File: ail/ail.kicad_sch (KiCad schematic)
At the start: 28 parts, among them J1 TS HV-, J2 TS HV+, J8 LED, Q8 FQD1N80TM, Q9 XP262N7002TR-G, U6 OP777

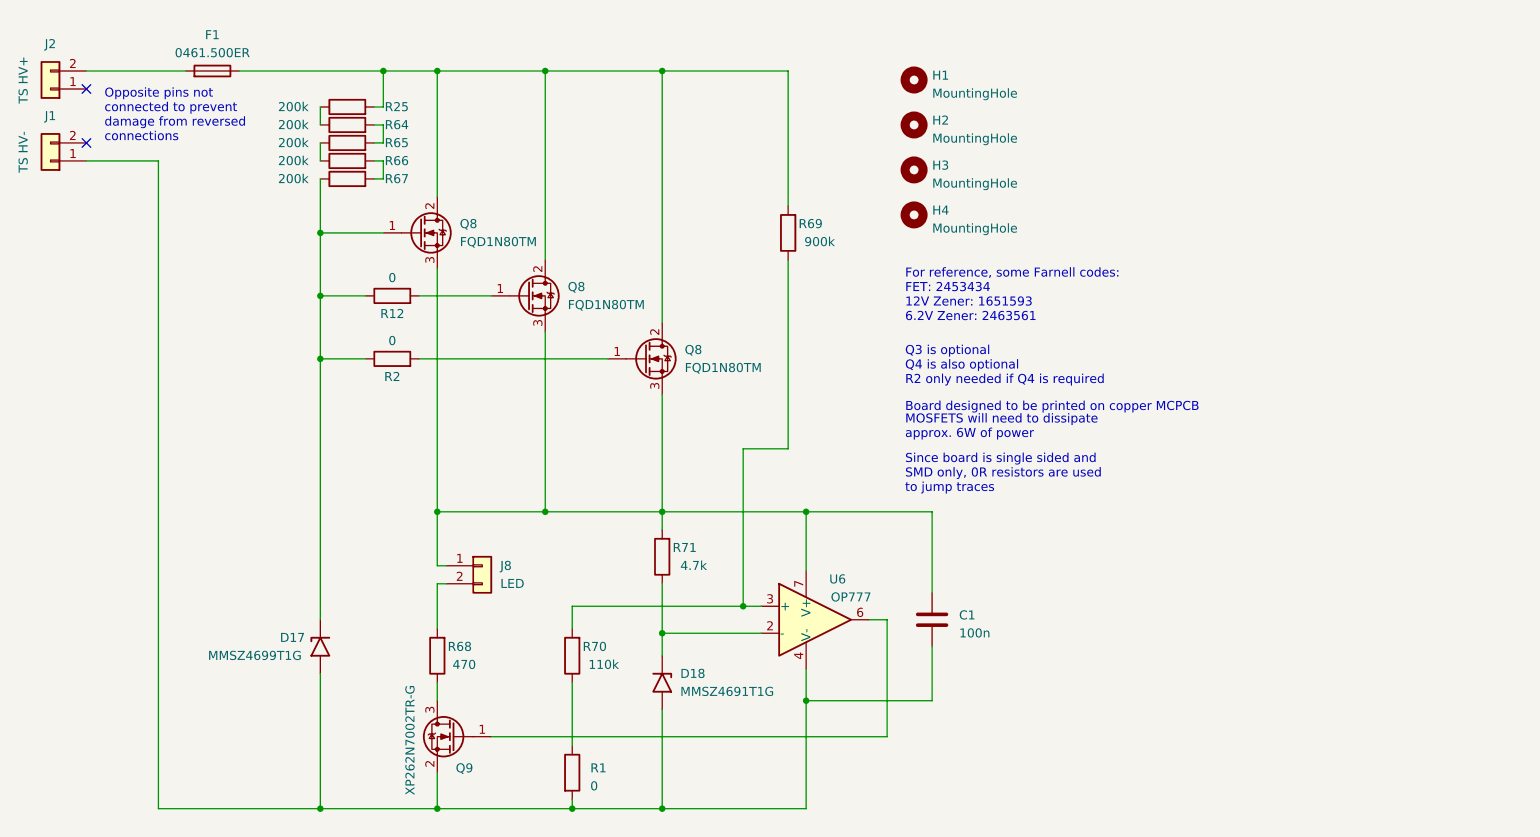
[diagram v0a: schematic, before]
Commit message: fix(ail): corrected remaining ERC errors
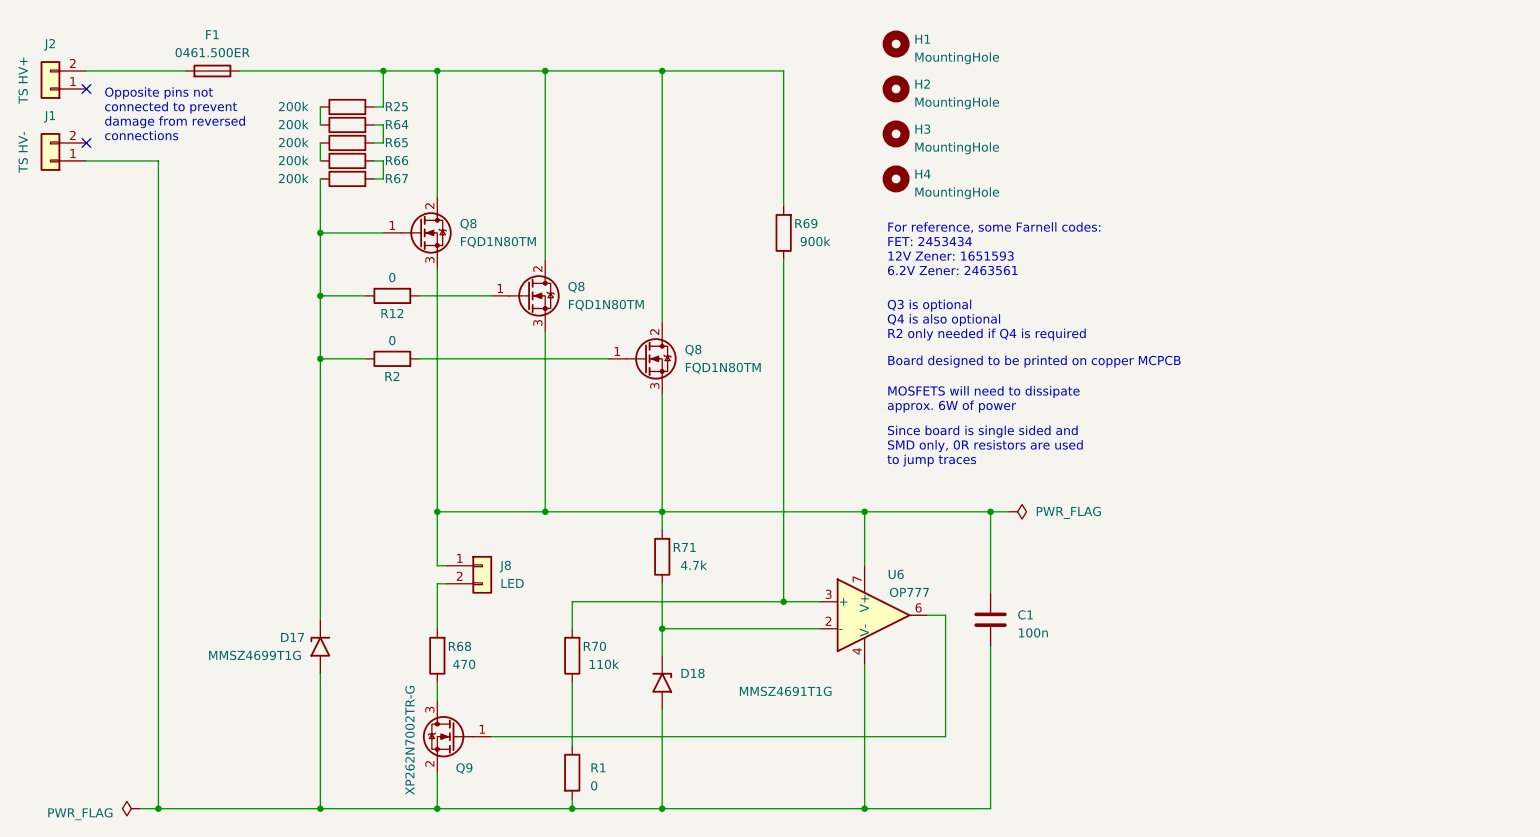
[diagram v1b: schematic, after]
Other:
- moved on the sheet: C1, H1, H2, H3, H4, R69, U6

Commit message: feat(ail): add copper pour to MOSFET drains (#95)
* Added copper pour to Q1-drain, removed R1

* fix(ail): remove track stubs

* wip(ail): attempt to fix clearance issues

not successfully...

* fix(ail): corrected clearance violation for isolation slot

* fix(ail): removed thermal relief for mosfet pour, increased size slightly

* fix(ail): replaced out of stock components

---------

Co-authored-by: Max O'Brien <max@maxobrien.co.uk>
Co-authored-by: Ray Wang <114954263+saltyboi2995@users.noreply.github.com>
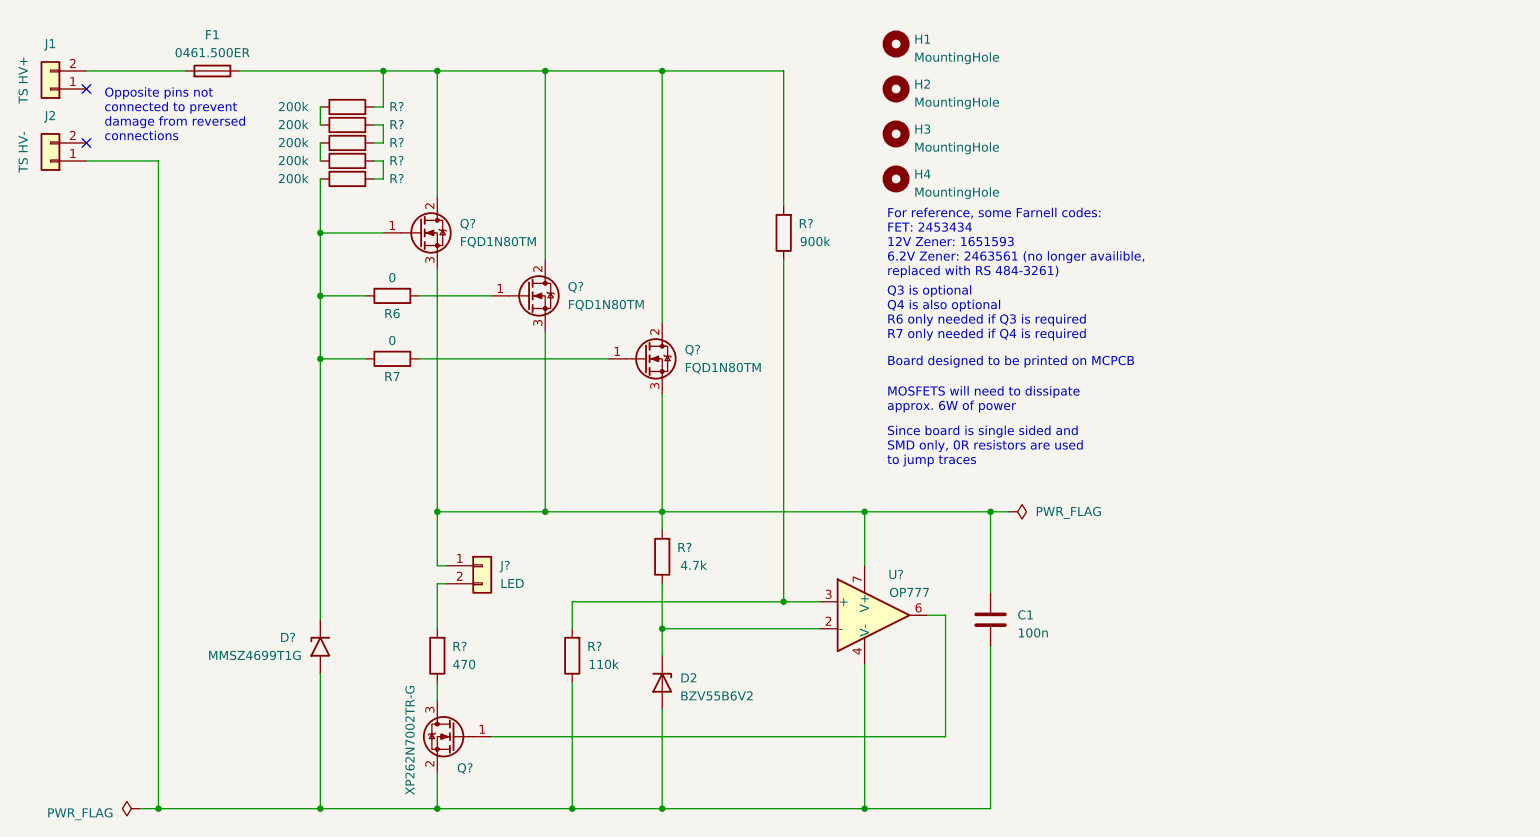
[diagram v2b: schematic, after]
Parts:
- removed D18: MMSZ4691T1G, Diode_SMD:D_SOD-123, symbol Diode:1N630xA
- removed R1: 0, Resistor_SMD:R_1206_3216Metric_Pad1.30x1.75mm_HandSolder, symbol Device:R
- added D2: BZV55B6V2, Diode_SMD:D_MiniMELF, symbol Diode:BZV55B6V2
- renumbered D17 to D?, J2 to J1, J1 to J2, J8 to J?, Q8 to Q?, Q9 to Q?, R12 to R6, R2 to R7, R65 to R?, R25 to R?, R67 to R?, R69 to R?, R71 to R?, R64 to R?, R68 to R?, R66 to R?, R70 to R?, U6 to U?
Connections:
- net at R?.1: now also C1.2, D?.2 (A2), J2.1 (Pin_1), Q?.2 (S), U?.4 (V-), D2.2 (A)
- net at R?.1, U?.2 (-): now also D2.1 (K)
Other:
- note added: "Board designed to be printed on MCPCB"
- note added: "For reference, some Farnell codes: FET: 2453434 12V Zener: 1651593 6.2V Zener: 2463561 (no longer availible, replaced with RS 484-3261)"
- note added: "Q3 is optional Q4 is also optional R6 only needed if Q3 is required R7 only needed if Q4 is required"
- note removed: "Board designed to be printed on copper MCPCB"
- note removed: "For reference, some Farnell codes: FET: 2453434 12V Zener: 1651593 6.2V Zener: 2463561"
- note removed: "Q3 is optional Q4 is also optional R2 only needed if Q4 is required"

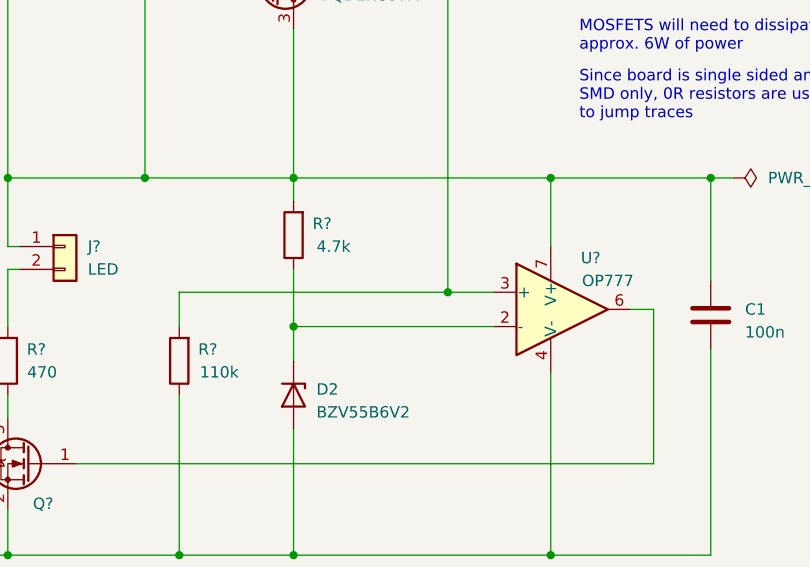
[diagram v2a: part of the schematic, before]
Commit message: Added message about missing clamp on non-inverting input of op-amp
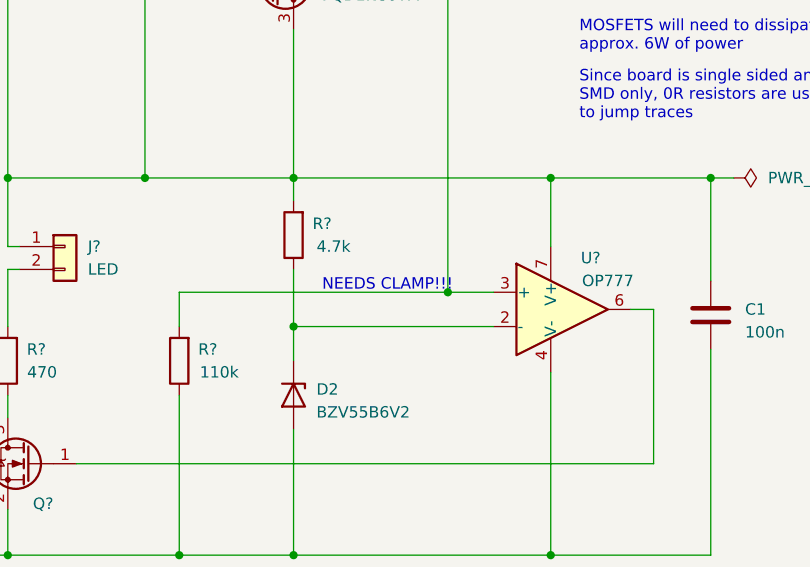
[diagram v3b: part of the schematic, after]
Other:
- note added: "NEEDS CLAMP!!!"
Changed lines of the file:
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@@
     (effects (font (size 1.27 1.27)) (justify left bottom))
+  )
+  (text "NEEDS CLAMP!!!" (at 109.855 97.79 0)
+    (effects (font (size 1.27 1.27) (color 255 0 0 1)) (justify left bottom))
   )
   (text "MOSFETS will need to dissipate \napprox. 6W of power"

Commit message: Added TODO tasks
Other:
- note added: "AIL TODO: - Clamp on op-amp - Choose heat sink"
- note removed: "NEEDS CLAMP!!!"
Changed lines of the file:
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@@
     (effects (font (size 1.27 1.27)) (justify left bottom))
   )
-  (text "NEEDS CLAMP!!!" (at 109.855 97.79 0)
+  (text "AIL TODO:\n- Clamp on op-amp\n- Choose heat sink" (at 205.105 38.1 0)
     (effects (font (size 1.27 1.27) (color 255 0 0 1)) (justify left bottom))
   )

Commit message: Updated schematics
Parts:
- removed R?: 900k, Resistor_SMD:R_0603_1608Metric, symbol Device:R
- added D?: MMSZ5239B, Diode_SMD:D_SOD-123, symbol Diode:1N630xA
- added R? (x4): 200k, Resistor_SMD:R_0805_2012Metric, symbol Device:R
- added R?: 100k, Resistor_SMD:R_0805_2012Metric, symbol Device:R
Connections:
- net at F1.1, Q?.2 (D), Q?.2 (D)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: now also R?.2
- net at R?.2, U?.3 (+): now also D?.1 (A1), R?.1
- net at C1.2, D2.2 (A), D?.2 (A2)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: now also D?.2 (A2)
- new net: R?.1, R?.1 (x2)
- new net: R?.2, R?.2 (x2)
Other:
- moved on the sheet: H1, H2, H3, H4

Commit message: Tweaks
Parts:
- added R? (x3): 10, Resistor_SMD:R_0603_1608Metric, symbol Device:R
- J?: footprint SUFST:Molex_Micro-Fit_3.0_43650-0214_1x02_P3.00mm_Horizontal -> Connector_Molex:Molex_Micro-Fit_3.0_43650-0224_1x02-1MP_P3.00mm_Vertical
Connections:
- net at C1.1, J?.1 (Pin_1), R?.2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: now also R?.1, R?.1, R?.1; no longer Q?.3 (S), Q?.3 (S), Q?.3 (S)
- new net: Q?.3 (S), R?.2 (x3)
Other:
- note added: "Balasting resistors balance current through MOSFETs"
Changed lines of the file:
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@@
     (stroke (width 0) (type default))
   )
-  (wire (pts (xy 106.68 68.58) (xy 106.68 85.09))
+  (wire (pts (xy 106.68 68.58) (xy 106.68 73.66))
     (stroke (width 0) (type default))
   )
@@
     (stroke (width 0) (type default))
   )
-  (wire (pts (xy 74.93 50.8) (xy 74.93 85.09))
+  (wire (pts (xy 74.93 50.8) (xy 74.93 73.66))
     (stroke (width 0) (type default))
   )
@@
     (stroke (width 0) (type default))
   )
+  (wire (pts (xy 106.68 81.28) (xy 106.68 85.09))
+    (stroke (width 0) (type default))
+  )
   (wire (pts (xy 123.825 22.86) (xy 123.825 31.115))
     (stroke (width 0) (type default))
@@
     (stroke (width 0) (type default))
   )
+  (wire (pts (xy 74.93 81.28) (xy 74.93 85.09))
+    (stroke (width 0) (type default))
+  )
   (wire (pts (xy 25.4 22.86) (xy 39.37 22.86))
     (stroke (width 0) (type default))
@@
     (stroke (width 0) (type default))
   )
+  (wire (pts (xy 90.17 81.28) (xy 90.17 85.09))
+    (stroke (width 0) (type default))
+  )
   (wire (pts (xy 35.56 127) (xy 35.56 35.56))
     (stroke (width 0) (type default))
@@
     (stroke (width 0) (type default))
   )
-  (wire (pts (xy 90.17 59.69) (xy 90.17 85.09))
+  (wire (pts (xy 90.17 59.69) (xy 90.17 73.66))
     (stroke (width 0) (type default))
   )
@@
     (effects (font (size 1.27 1.27)) (justify left bottom))
   )
+  (text "Balasting resistors\nbalance current\nthrough MOSFETs"
+    (at 71.755 90.17 90)
+    (effects (font (size 1.27 1.27)) (justify left bottom))
+  )
   (symbol (lib_id "SUFST:FQD1N80TM") (at 72.39 45.72 0) (unit 1)
     (in_bom yes) (on_board yes) (dnp no) (fields_autoplaced)
@@
     )
   )
+  (symbol (lib_id "Device:R") (at 106.68 77.47 180) (unit 1)
+    (in_bom yes) (on_board yes) (dnp no)
+    (property "Reference" "R?" (at 109.855 76.2 0)
+      (effects (font (size 1.27 1.27)))
+    )
+    (property "Value" "10" (at 111.125 78.74 0)
+      (effects (font (size 1.27 1.27)))
+    )
+    (property "Footprint" "Resistor_SMD:R_0603_1608Metric" (at 108.458 77.47 90)
+      (effects (font (size 1.27 1.27)) hide)
+    )
+    (property "Datasheet" "~" (at 106.68 77.47 0)
+      (effects (font (size 1.27 1.27)) hide)
+    )
+    (pin "1")
+    (pin "2")
+    (instances
+      (project "precharge"
+        (path "/c338d9d7-bd26-41c6-bf7b-7bcaecdc6d24/9efa549b-079b-4747-bbda-5d5b1defcab0"
+          (reference "R?") (unit 1)
+        )
+      )
+      (project "ail"
+        (path "/db6c17fc-6072-4138-918a-66af94710d5a"
+          (reference "R18") (unit 1)
+        )
+      )
+    )
+  )
   (symbol (lib_id "power:PWR_FLAG") (at 155.575 85.09 270) (unit 1)
     (in_bom yes) (on_board yes) (dnp no)
@@
         (path "/db6c17fc-6072-4138-918a-66af94710d5a"
           (reference "#FLG02") (unit 1)
+        )
+      )
+    )
+  )
+  (symbol (lib_id "Device:R") (at 74.93 77.47 180) (unit 1)
+    (in_bom yes) (on_board yes) (dnp no)
+    (property "Reference" "R?" (at 78.105 76.2 0)
+      (effects (font (size 1.27 1.27)))
+    )
+    (property "Value" "10" (at 79.375 78.74 0)
+      (effects (font (size 1.27 1.27)))
+    )
+    (property "Footprint" "Resistor_SMD:R_0603_1608Metric" (at 76.708 77.47 90)
+      (effects (font (size 1.27 1.27)) hide)
+    )
+    (property "Datasheet" "~" (at 74.93 77.47 0)
+      (effects (font (size 1.27 1.27)) hide)
+    )
+    (pin "1")
+    (pin "2")
+    (instances
+      (project "precharge"
+        (path "/c338d9d7-bd26-41c6-bf7b-7bcaecdc6d24/9efa549b-079b-4747-bbda-5d5b1defcab0"
+          (reference "R?") (unit 1)
+        )
+      )
+      (project "ail"
+        (path "/db6c17fc-6072-4138-918a-66af94710d5a"
+          (reference "R11") (unit 1)
         )
       )
@@
       (effects (font (size 1.27 1.27)) (justify left))
     )
-    (property "Footprint" "SUFST:Molex_Micro-Fit_3.0_43650-0214_1x02_P3.00mm_Horizontal" (at 81.28 92.71 0)
+    (property "Footprint" "Connector_Molex:Molex_Micro-Fit_3.0_43650-0224_1x02-1MP_P3.00mm_Vertical" (at 81.28 92.71 0)
       (effects (font (size 1.27 1.27)) hide)
     )
@@
         )
       )
+    )
+  )
+  (symbol (lib_id "Device:R") (at 90.17 77.47 180) (unit 1)
+    (in_bom yes) (on_board yes) (dnp no)
+    (property "Reference" "R?" (at 93.345 76.2 0)
+      (effects (font (size 1.27 1.27)))
+    )
+    (property "Value" "10" (at 94.615 78.74 0)
+      (effects (font (size 1.27 1.27)))
+    )
+    (property "Footprint" "Resistor_SMD:R_0603_1608Metric" (at 91.948 77.47 90)
+      (effects (font (size 1.27 1.27)) hide)
+    )
+    (property "Datasheet" "~" (at 90.17 77.47 0)
+      (effects (font (size 1.27 1.27)) hide)
+    )
+    (pin "1")
+    (pin "2")
+    (instances
+      (project "precharge"
+        (path "/c338d9d7-bd26-41c6-bf7b-7bcaecdc6d24/9efa549b-079b-4747-bbda-5d5b1defcab0"
+          (reference "R?") (unit 1)
+        )
+      )
+      (project "ail"
+        (path "/db6c17fc-6072-4138-918a-66af94710d5a"
+          (reference "R17") (unit 1)
+        )
+      )

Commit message: AIL PCB done, pending review
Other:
- note removed: "AIL TODO: - Clamp on op-amp - Choose heat sink"
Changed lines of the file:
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@@
     (title "Accumulator Indicator Light")
     (date "2023-04-17")
-    (rev "1.0.1")
+    (rev "1.0.2")
     (company "SUFST")
     (comment 1 "STAG 9")
@@
     (effects (font (size 1.27 1.27)) (justify left bottom))
   )
-  (text "AIL TODO:\n- Clamp on op-amp\n- Choose heat sink" (at 205.105 38.1 0)
-    (effects (font (size 1.27 1.27) (color 255 0 0 1)) (justify left bottom))
-  )
   (text "MOSFETS will need to dissipate \napprox. 6W of power"

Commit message: Some stuff
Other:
- note added: "MOSFET replacement: IPD80R4K5P7"
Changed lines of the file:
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@@
+    (effects (font (size 1.27 1.27)) (justify left bottom))
+  )
+  (text "MOSFET replacement: IPD80R4K5P7" (at 91.44 17.145 0)
     (effects (font (size 1.27 1.27)) (justify left bottom))
   )
